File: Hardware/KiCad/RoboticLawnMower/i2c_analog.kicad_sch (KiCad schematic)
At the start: 24 parts, among them J14 ADC 1, J15 ADC 2, U8 ADS1115IDGS, U9 ADS1115IDGS

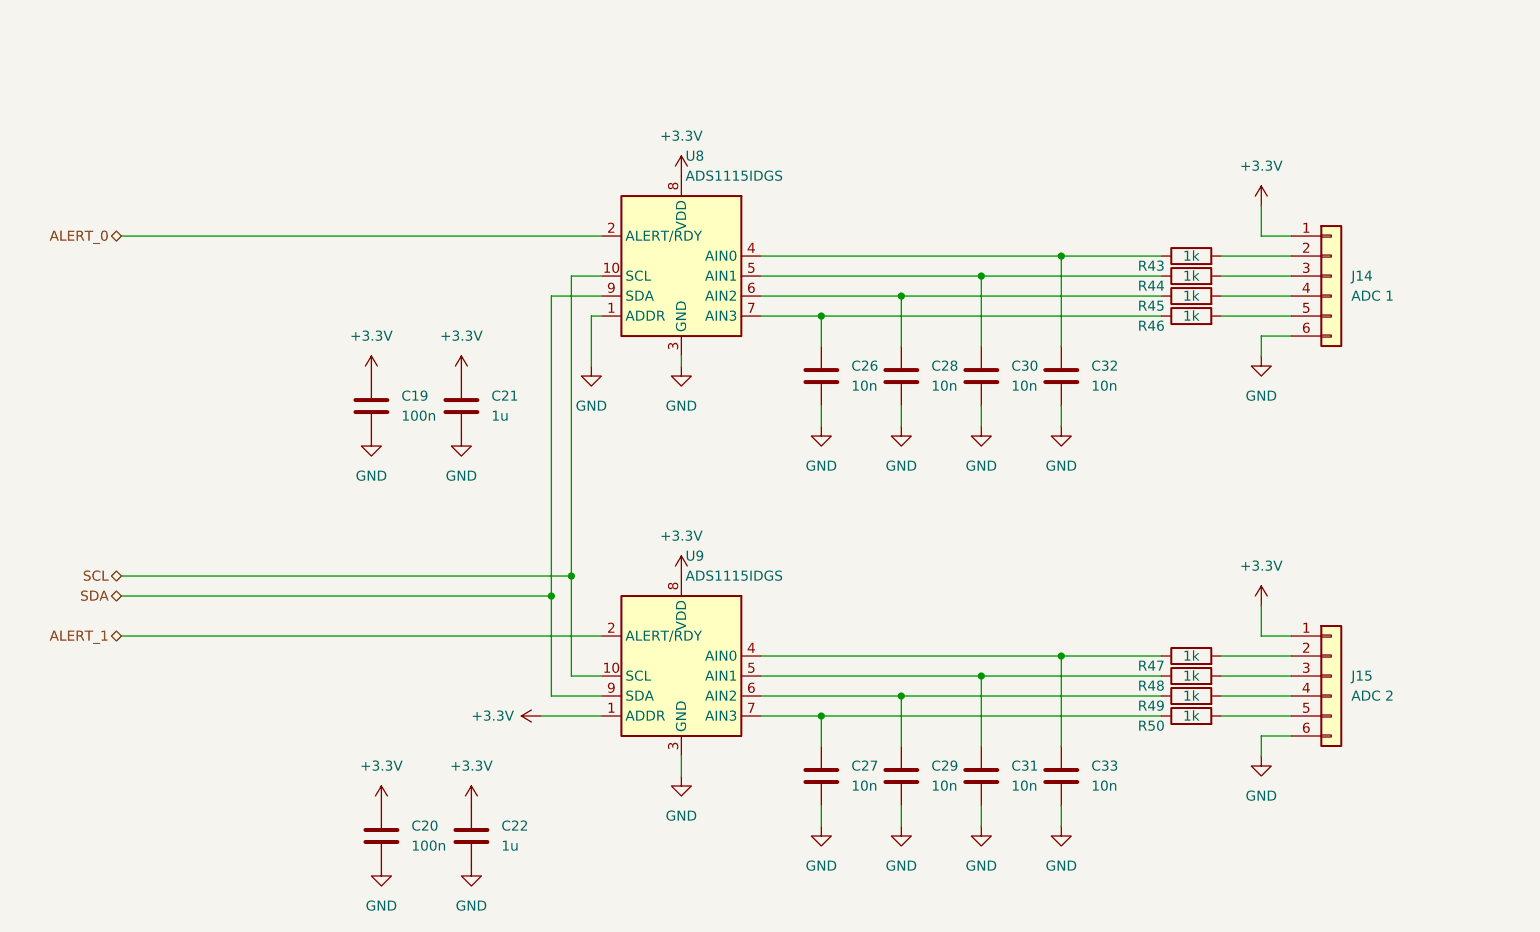
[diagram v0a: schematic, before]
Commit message: Redesign: - Controller - I2C pinning geändert - uvm
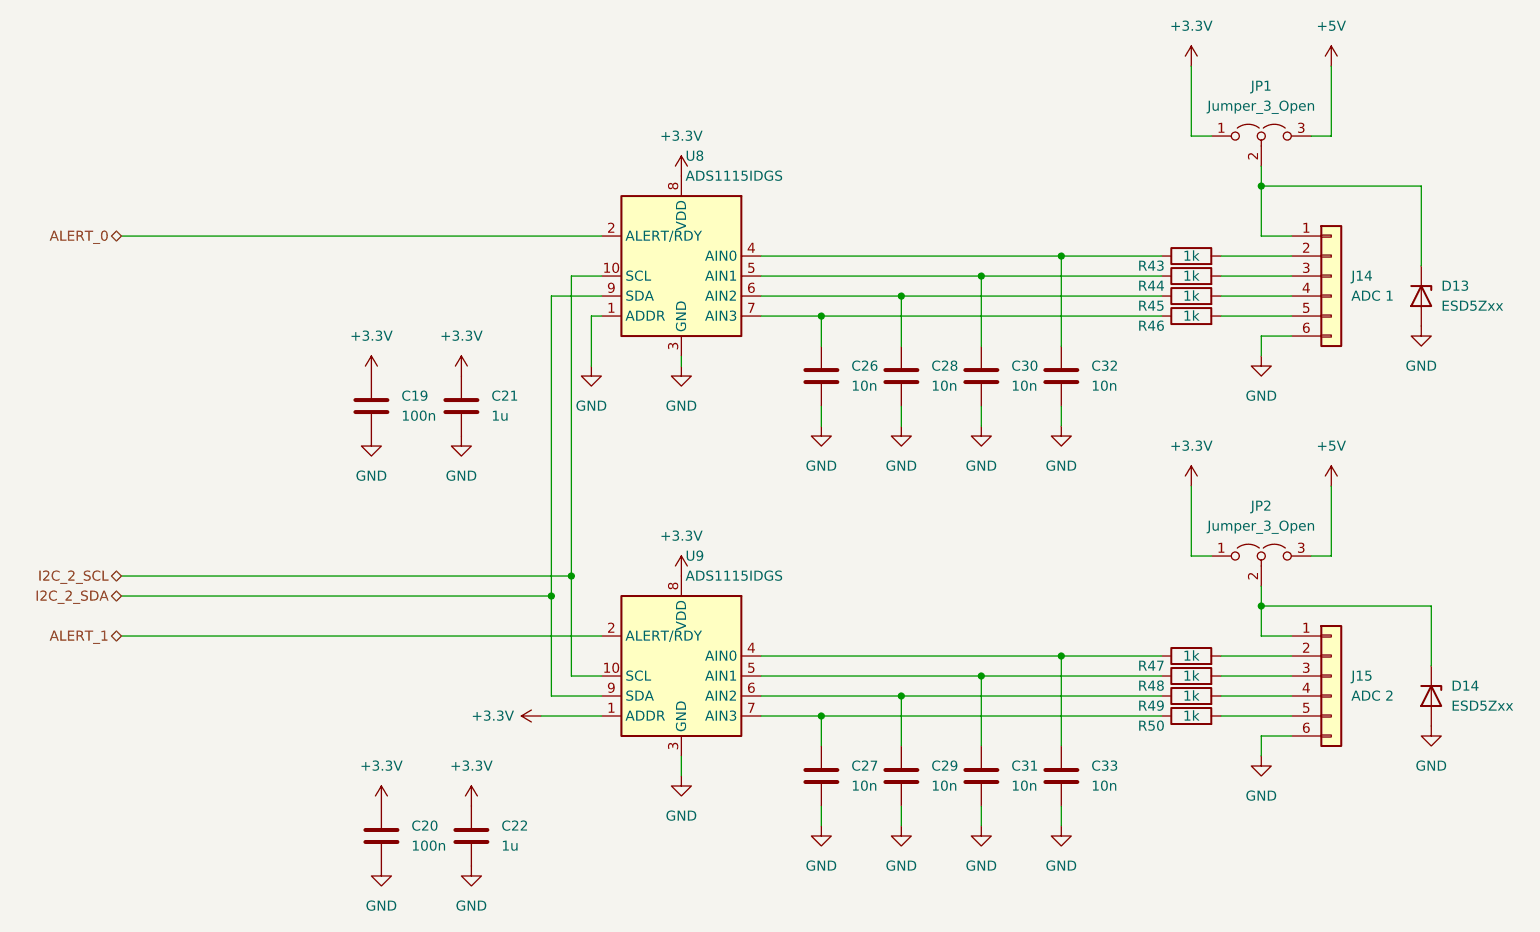
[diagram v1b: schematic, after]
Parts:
- added D13, D14: ESD5Zxx, Diode_SMD:D_SOD-523, symbol Diode:ESD5Zxx
- added JP1, JP2: Jumper_3_Open, Jumper:SolderJumper-3_P1.3mm_Bridged12_RoundedPad1.0x1.5mm, symbol Jumper:Jumper_3_Open
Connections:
- net +3.3V: now also JP1.1 (A), JP2.1 (A); no longer J14.1 (Pin_1), J15.1 (Pin_1)
- net GND: now also D13.2 (A), D14.2 (A)
- net SCL renamed I2C_2_SCL
- net SDA renamed I2C_2_SDA
- new net: D13.1 (K), J14.1 (Pin_1), JP1.2 (C)
- new net: D14.1 (K), J15.1 (Pin_1), JP2.2 (C)
- new net +5V: JP1.3 (B), JP2.3 (B)
